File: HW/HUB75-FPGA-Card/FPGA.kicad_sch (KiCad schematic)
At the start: 13 parts, among them U2 T20Q100F3

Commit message: add usb audio implementation
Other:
- moved on the sheet: C4, R1, R17, R2, R3, R4, R5, R6, U2A, U2B, U2D

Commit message: finish up schematic and begin routing
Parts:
- added C1, C12, C14, C15, C16, C17, C18, C20, C21, C22, C5, C6, C7, C8, C9: 100n, Capacitor_SMD:C_0603_1608Metric, symbol Device:C
- added C10, C11, C23, C24, C4: 1u, Capacitor_SMD:C_0603_1608Metric, symbol Device:C
- added C13: 4.7u, Capacitor_SMD:C_0603_1608Metric, symbol Device:C
- added C3: 10u, Capacitor_SMD:C_0603_1608Metric, symbol Device:C
- added FB1: FerriteBead_Small, Resistor_SMD:R_0603_1608Metric, symbol Device:FerriteBead_Small
- added J1: Conn_02x04_Odd_Even, Connector_PinHeader_2.54mm:PinHeader_2x04_P2.54mm_Vertical, symbol Connector_Generic:Conn_02x04_Odd_Even
- added U13: AP2112K-1.2, Package_TO_SOT_SMD:SOT-23-5, symbol Regulator_Linear:AP2112K-1.2
- added U2: XC6206PxxxMR, Package_TO_SOT_SMD:SOT-23-3, symbol Regulator_Linear:XC6206PxxxMR
- added X1: ECS-2520MV-xxx-xx, Oscillator:Oscillator_SMD_ECS_2520MV-xxx-xx-4Pin_2.5x2.0mm, symbol Oscillator:ECS-2520MV-xxx-xx
- C2: renamed from C4; footprint (none) -> Capacitor_SMD:C_0603_1608Metric
- R1, R10, R11, R2, R3, R4, R5, R6, R8, R9: footprint (none) -> Resistor_SMD:R_0603_1608Metric
- R10: renamed from R17; footprint (none) -> Resistor_SMD:R_0603_1608Metric
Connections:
- net +3V3: now also U2.11 (VCCIO1A_1B_1C), U2.21 (VCCIO1A_1B_1C), U2.34 (VCCIO4B), U2.42 (VCCIO4A), U2.60 (VCCIO3D_3E), U2.69 (VCCIO3B_3C), U2.76 (VCCIO3A), U2.96 (VCCIO1D_1E), C1.1, C11.1, C14.1, C15.1, C16.1, C17.1, C18.1, C20.1, C21.1, C22.1, C23.1, J1.2 (Pin_2), U13.1 (VIN), U13.3 (EN), U2.2 (VO), X1.4 (VDD)
- net B1: now also U2.2 (GPIOL_41_CDI9)
- net B2: now also U2.100 (GPIOL_46)
- net B3: now also U2.74 (GPIOR_87_CDI29)
- net B4: now also U2.79 (GPIOR_77_PLLIN1)
- net BLANK: now also U2.87 (GPIOL_73_EXTFB1_CDI15)
- net CLKOUT: now also U2.89 (GPIOL_72_EXTFB0_CDI14)
- net CLK_12MHZ: now also U2.14 (GPIOL_13_CDI3)
- net CLK_60MHZ: now also U2.7 (GPIOL_24_CLK0)
- net D0: now also U2.41 (GPIOB_RXN00)
- net D1: now also U2.40 (GPIOB_RXP00)
- net D2: now also U2.38 (GPIOB_TXN10)
- net D3: now also U2.37 (GPIOB_TXP10)
- net D4: now also U2.33 (GPIOB_TXN04)
- net D5: now also U2.32 (GPIOB_TXP04)
- net D6: now also U2.30 (GPIOB_TXN01)
- net D7: now also U2.29 (GPIOB_TXP01)
- net G1: now also U2.3 (GPIOL_40_CDI8)
- net G2: now also U2.99 (GPIOL_54_CDI11)
- net G3: now also U2.77 (GPIOR_79_EXTFB1_CDI30)
- net G4: now also U2.78 (GPIOR_78_EXTFB0_CDI31)
- net GND: now also C1.2, C10.2, C11.2, C12.2, C13.2, C14.2, C15.2, C16.2, C17.2, C18.2, C20.2, C21.2, C22.2, C23.2, C24.2, C3.2, C4.2, C5.2, C6.2, C7.2, C8.2, C9.2, J1.7 (Pin_7), J1.8 (Pin_8), U13.2 (GND), U2.1 (GND), X1.2 (GND)
- net LAT: now also U2.88 (GPIOL_71_NSTATUS)
- net R1: now also U2.4 (GPIOL_32_CTRL4_CDI7)
- net R2: now also U2.98 (GPIOL_53_CDI10)
- net R3: now also U2.73 (GPIOR_88_CDI28)
- net R4: now also U2.80 (GPIOR_76_PLLIN0)
- net ROW_CLK: now also U2.93 (GPIOL_69_CBSEL1)
- net ROW_DATA: now also U2.92 (GPIOL_70_CBSEL0)
- net STRIP1: now also U2.95 (GPIOL_66_CDI12)
- net STRIP2: now also U2.94 (GPIOL_67_CDI13)
- net STRIP3: now also U2.86 (GPIOL_74_PLLIN0)
- net STRIP4: now also U2.85 (GPIOL_75_PLLIN1)
- net ~{OE}: now also U2.5 (GPIOL_31_CLK7_CDI6)
- net ~{RD}: now also U2.9 (GPIOL_21_CTRL1_CDI5)
- net ~{RXF}: now also U2.22 (GPIOL_05_CSO)
- net ~{TXE}: now also U2.10 (GPIOL_20_CTRL0_CDI4)
- net ~{WR}: now also U2.8 (GPIOL_12_CDI2)
- net CRESET_N: now reaches C2.1, R10.2, U2.20 (CRESET_N)
- net CRESET_N: now also J1.6 (Pin_6)
- net +1V2: now reaches U2.15 (VCC)
- net +1V2: now also U2.31 (VCC), U2.45 (VCC), U2.64 (VCC), U2.75 (VCC), U2.82 (VCC), U2.83 (VCC), U2.91 (VCC), C24.1, C3.1, C4.1, C5.1, C6.1, C7.1, C8.1, C9.1, FB1.1, U13.5 (VOUT)
- net at U2.50 (VCCA_BR): now also U2.72 (VCCA_TR), U2.84 (VCCA_TL), C12.1, C13.1, FB1.2
- net at U2.54 (GPIOR_157_PLLIN): now also X1.3 (OUT)
- net TDO: now reaches U2.12 (TDO)
- net TDO: now also J1.1 (Pin_1)
- net at U2.13 (TCK): now also J1.3 (Pin_3)
- net TMS: now reaches U2.16 (TMS)
- net TMS: now also J1.5 (Pin_5)
- net TDI: now reaches U2.17 (TDI)
- net TDI: now also J1.4 (Pin_4)
- new net +5V: C10.1, U2.3 (VI)
- no-connect marks 19 -> 12
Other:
- note added: "JTAG"
- note added: "Not recommended but functional on their official devboard"
- note added: "Oscillator"
- note added: "Power"
- note added: "TCK"
- note removed: "Maybe should use power supervisor instead"
- moved on the sheet: R10, R11, R6, R8, R9, U2A, U2C, U2D

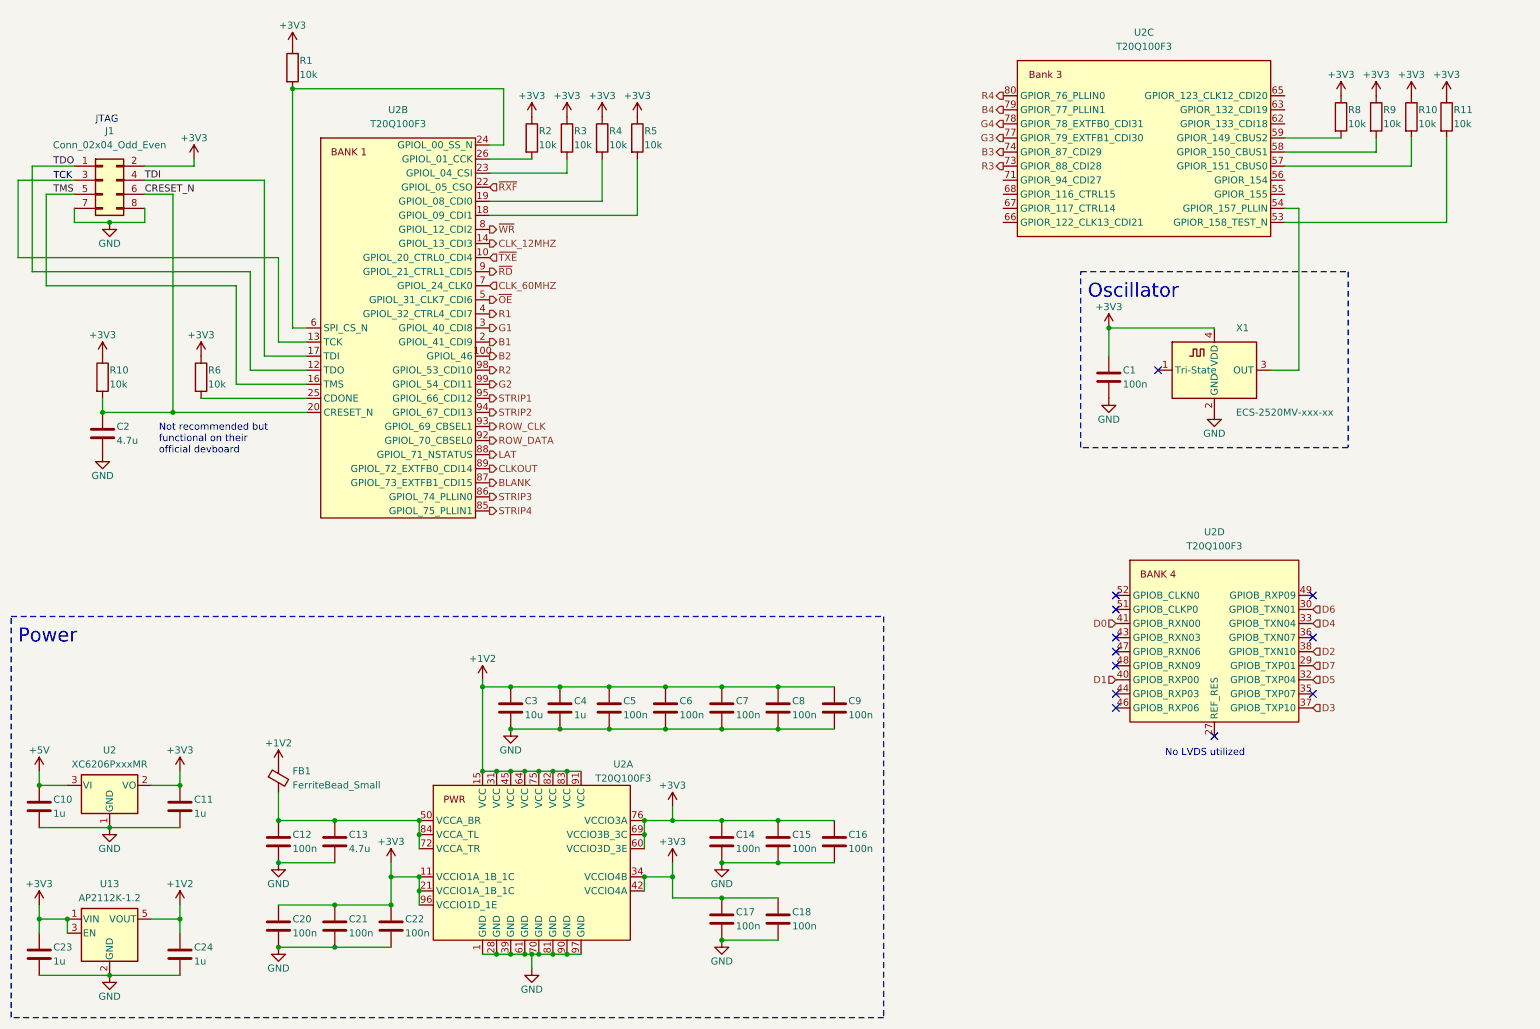
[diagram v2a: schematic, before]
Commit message: finalize pcb and generate production files for first run
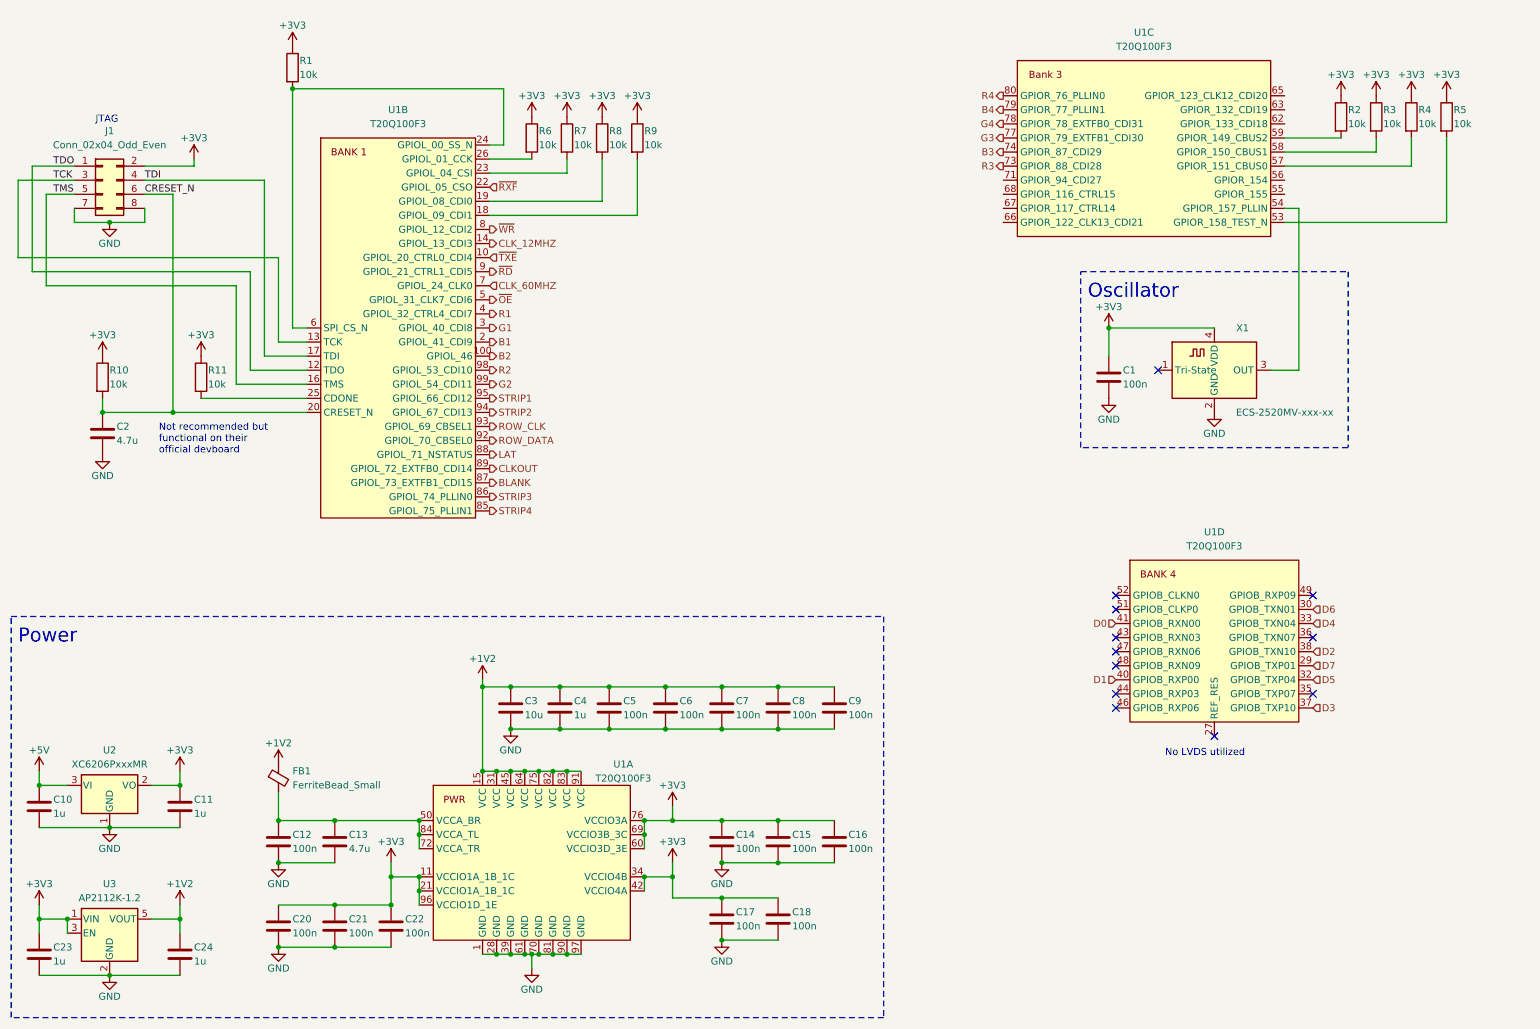
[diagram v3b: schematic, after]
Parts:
- renumbered R6 to R11, R8 to R2, R9 to R3, R10 to R4, R11 to R5, R2 to R6, R3 to R7, R4 to R8, R5 to R9, U2 to U1, U13 to U3
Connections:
- net TCK: now reaches J1.3 (Pin_3), U1.13 (TCK)
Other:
- note removed: "TCK"

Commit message: saving hardware progress
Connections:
- net GND: no longer J1.7 (Pin_7)
- net SS: now reaches R1.2, U1.24 (GPIOL_00_SS_N), U1.6 (SPI_CS_N)
- net SS: now also J1.7 (Pin_7)
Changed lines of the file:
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@@
   (junction (at 31.75 161.29) (diameter 0) (color 0 0 0 0)
   )
-  (junction (at 31.75 52.07) (diameter 0) (color 0 0 0 0)
-  )
   (junction (at 132.08 143.51) (diameter 0) (color 0 0 0 0)
   )
@@
   )
   (junction (at 43.18 86.36) (diameter 0) (color 0 0 0 0)
+  )
+  (junction (at 64.77 55.88) (diameter 0) (color 0 0 0 0)
   )
   (junction (at 142.24 181.61) (diameter 0) (color 0 0 0 0)
@@
     (stroke (width 0) (type default))
   )
+  (wire (pts (xy 22.86 55.88) (xy 64.77 55.88))
+    (stroke (width 0) (type default))
+  )
   (wire (pts (xy 54.61 63.5) (xy 54.61 81.28))
     (stroke (width 0) (type default))
@@
     (stroke (width 0) (type default))
   )
-  (wire (pts (xy 38.1 52.07) (xy 38.1 49.53))
-    (stroke (width 0) (type default))
-  )
   (wire (pts (xy 31.75 187.96) (xy 44.45 187.96))
     (stroke (width 0) (type default))
@@
     (stroke (width 0) (type default))
   )
+  (wire (pts (xy 25.4 49.53) (xy 22.86 49.53))
+    (stroke (width 0) (type default))
+  )
   (wire (pts (xy 121.92 143.51) (xy 132.08 143.51))
     (stroke (width 0) (type default))
   )
-  (wire (pts (xy 25.4 49.53) (xy 25.4 52.07))
-    (stroke (width 0) (type default))
-  )
   (wire (pts (xy 113.03 143.51) (xy 121.92 143.51))
     (stroke (width 0) (type default))
@@
     (stroke (width 0) (type default))
   )
-  (wire (pts (xy 64.77 71.12) (xy 64.77 27.94))
+  (wire (pts (xy 64.77 71.12) (xy 64.77 55.88))
     (stroke (width 0) (type default))
   )
@@
     (stroke (width 0) (type default))
   )
+  (wire (pts (xy 64.77 55.88) (xy 64.77 27.94))
+    (stroke (width 0) (type default))
+  )
   (wire (pts (xy 19.05 151.13) (xy 19.05 153.67))
     (stroke (width 0) (type default))
@@
     (stroke (width 0) (type default))
   )
-  (wire (pts (xy 31.75 52.07) (xy 38.1 52.07))
-    (stroke (width 0) (type default))
-  )
-  (wire (pts (xy 25.4 52.07) (xy 31.75 52.07))
-    (stroke (width 0) (type default))
-  )
   (wire (pts (xy 44.45 151.13) (xy 44.45 153.67))
     (stroke (width 0) (type default))
@@
   )
   (wire (pts (xy 104.14 184.15) (xy 106.68 184.15))
+    (stroke (width 0) (type default))
+  )
+  (wire (pts (xy 22.86 49.53) (xy 22.86 55.88))
     (stroke (width 0) (type default))
   )
@@
   )
   (label "TDI" (at 38.1 44.45 0) (fields_autoplaced)
+    (effects (font (size 1.27 1.27)) (justify left bottom))
+  )
+  (label "SS" (at 22.86 49.53 0) (fields_autoplaced)
     (effects (font (size 1.27 1.27)) (justify left bottom))
   )
@@
     )
   )
-  (symbol (lib_id "power:GND") (at 31.75 52.07 0) (unit 1)
-    (in_bom yes) (on_board yes) (dnp no)
-    (property "Reference" "#PWR011" (at 31.75 58.42 0)
-      (effects (font (size 1.27 1.27)) hide)
-    )
-    (property "Value" "GND" (at 31.75 55.88 0)
-      (effects (font (size 1.27 1.27)))
-    )
-    (property "Footprint" "" (at 31.75 52.07 0)
-      (effects (font (size 1.27 1.27)) hide)
-    )
-    (property "Datasheet" "" (at 31.75 52.07 0)
-      (effects (font (size 1.27 1.27)) hide)
-    )
+  (symbol (lib_id "power:GND") (at 38.1 49.53 0) (unit 1)
+    (in_bom yes) (on_board yes) (dnp no)
+    (property "Reference" "#PWR011" (at 38.1 55.88 0)
+      (effects (font (size 1.27 1.27)) hide)
+    )
+    (property "Value" "GND" (at 38.1 53.34 0)
+      (effects (font (size 1.27 1.27)))
+    )
+    (property "Footprint" "" (at 38.1 49.53 0)
+      (effects (font (size 1.27 1.27)) hide)
+    )
+    (property "Datasheet" "" (at 38.1 49.53 0)
+      (effects (font (size 1.27 1.27)) hide)
+    )

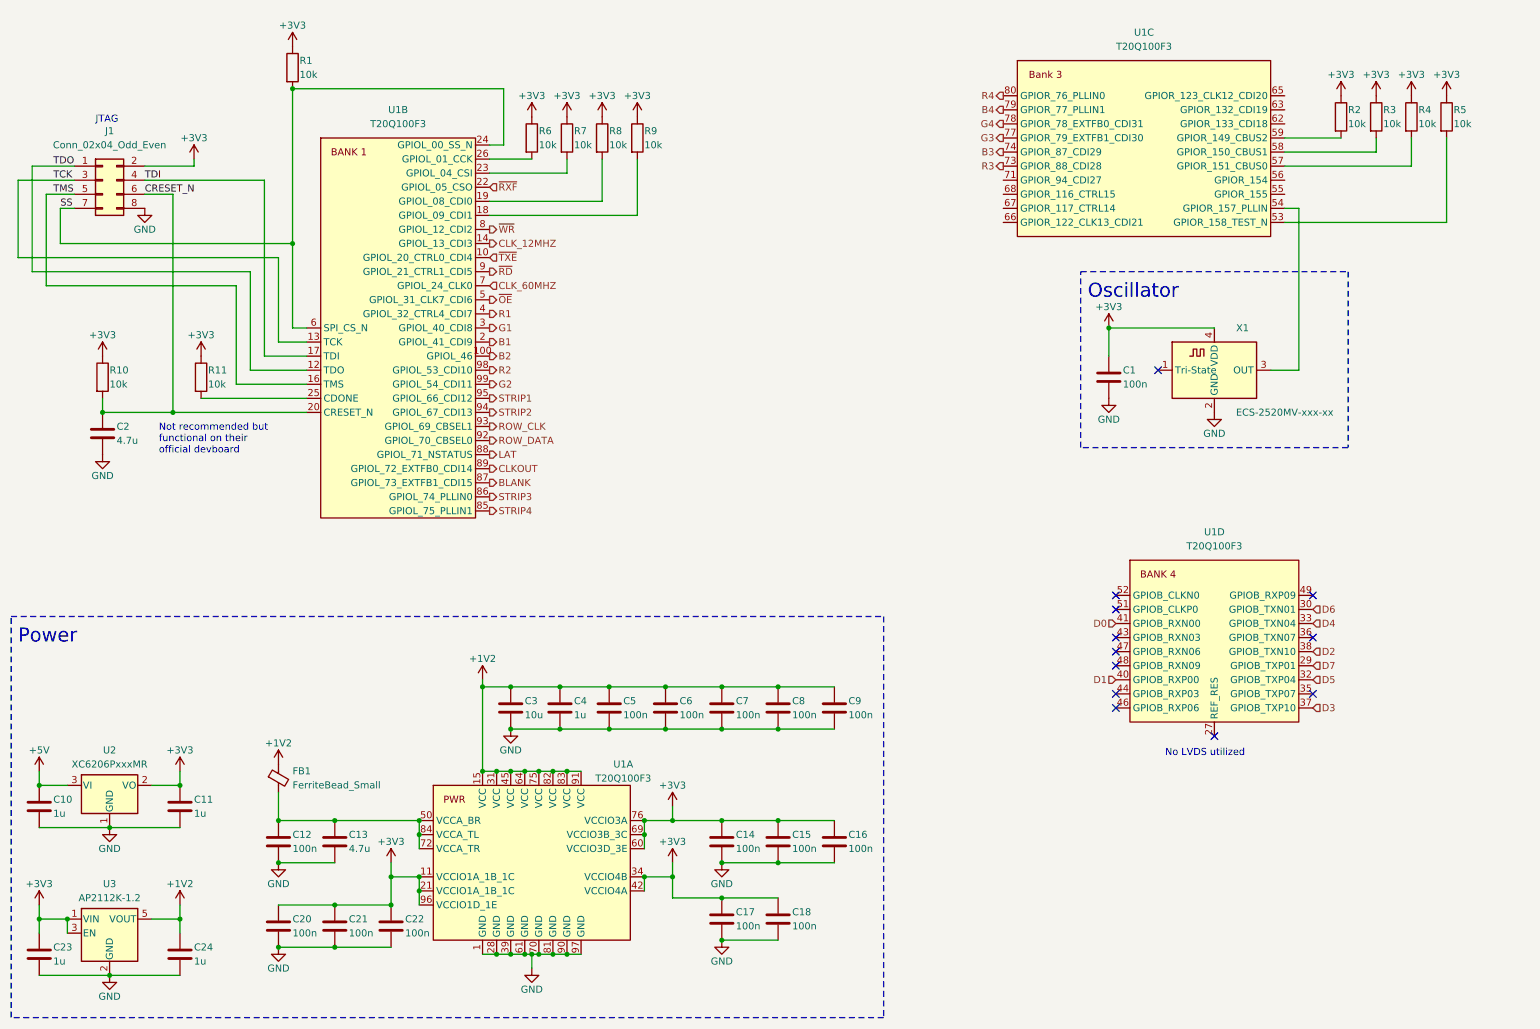
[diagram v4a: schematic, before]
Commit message: initial v1.1 board layout
still needs rp2040 pins routed
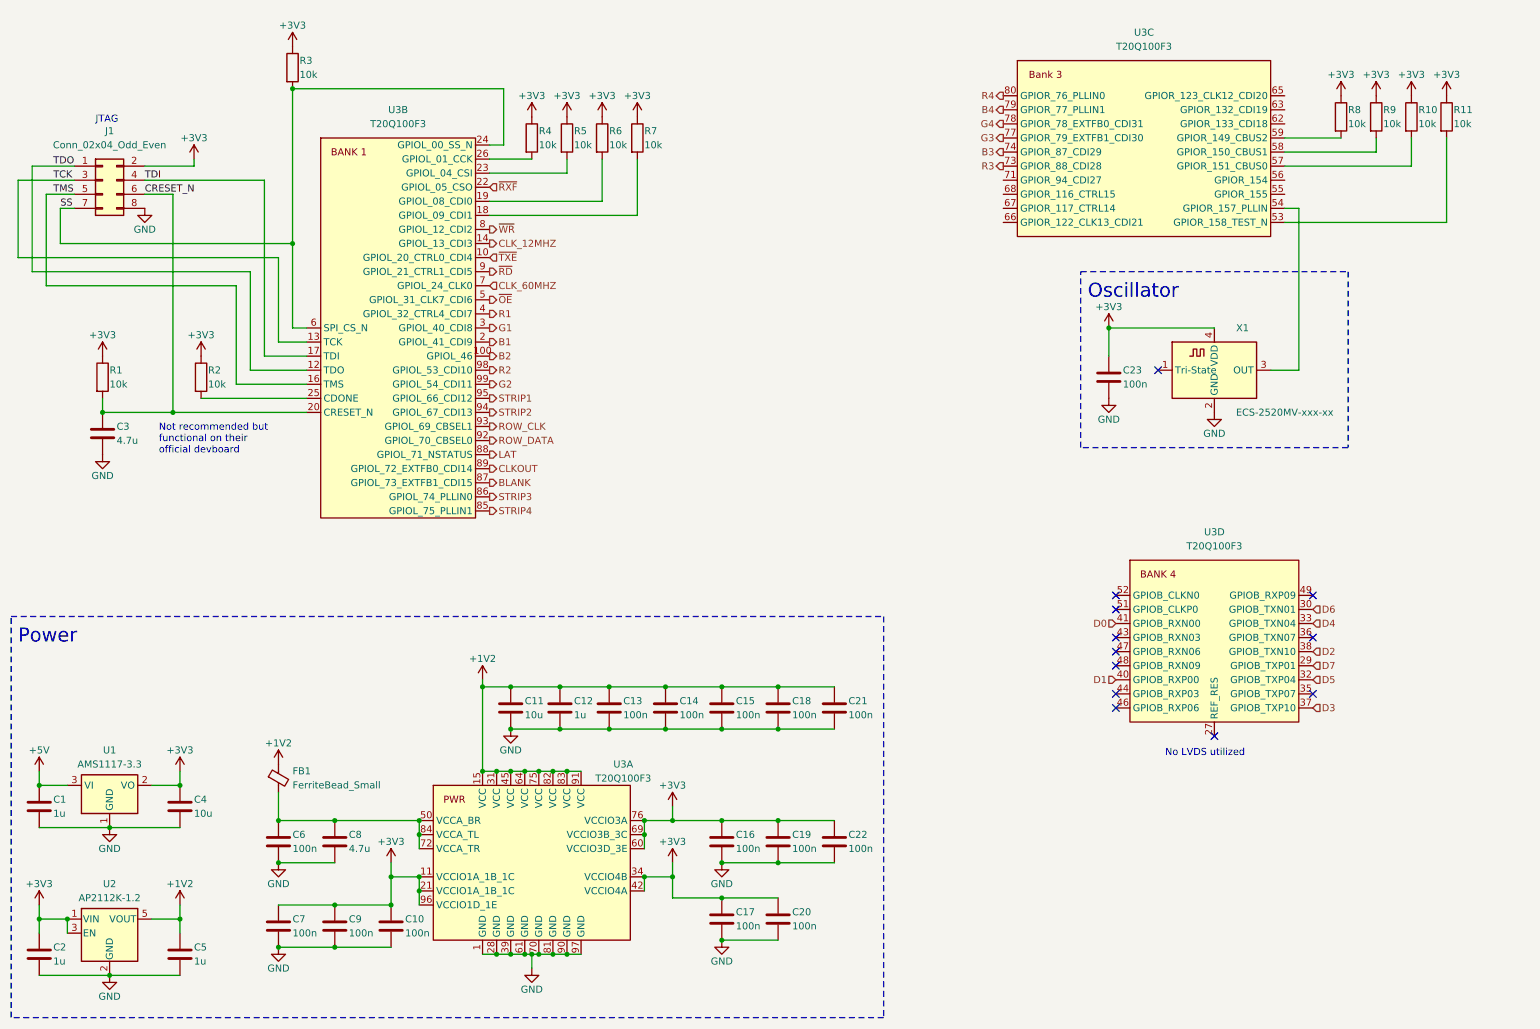
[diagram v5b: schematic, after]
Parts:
- removed U2: XC6206PxxxMR, Package_TO_SOT_SMD:SOT-23-3, symbol Regulator_Linear:XC6206PxxxMR
- added U1: AMS1117-3.3, Package_TO_SOT_SMD:SOT-223-3_TabPin2, symbol Regulator_Linear:AMS1117-3.3
- C4: renamed from C11; value 1u -> 10u
- renumbered C10 to C1, C22 to C10, C3 to C11, C4 to C12, C5 to C13, C6 to C14, C7 to C15, C14 to C16, C8 to C18, C15 to C19, C23 to C2, C18 to C20, C9 to C21, C16 to C22, C1 to C23, C2 to C3, C24 to C5, C12 to C6, C20 to C7, C13 to C8, C21 to C9, R10 to R1, R4 to R10, R5 to R11, R11 to R2, R1 to R3, R6 to R4, R7 to R5, R8 to R6, R9 to R7, R2 to R8, R3 to R9, U3 to U2, U1 to U3
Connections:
- net +3V3: now also U1.2 (VO)
- net +5V: now also U1.3 (VI)
- net GND: now also U1.1 (GND)
